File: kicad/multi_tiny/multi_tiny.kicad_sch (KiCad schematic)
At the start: 5 parts, among them U1 ATtiny85-20P, U2 ATtiny85-20P, U3 ATtiny85-20P, U4 CD4052B, U5 CD4052B

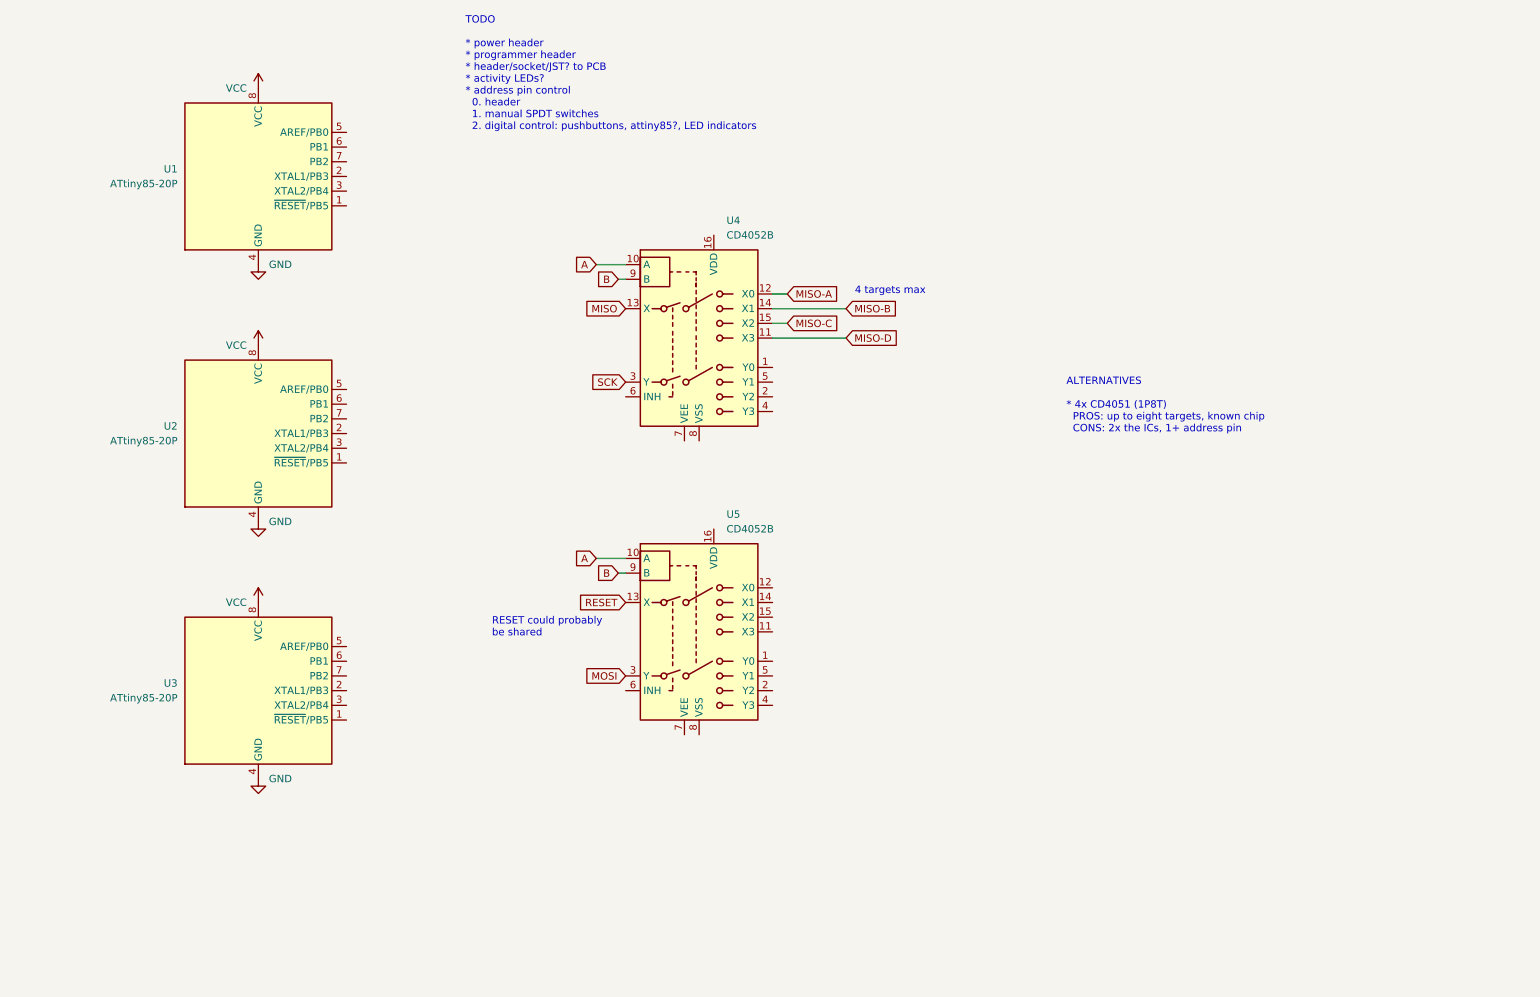
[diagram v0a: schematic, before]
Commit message: Complete MVP schematic
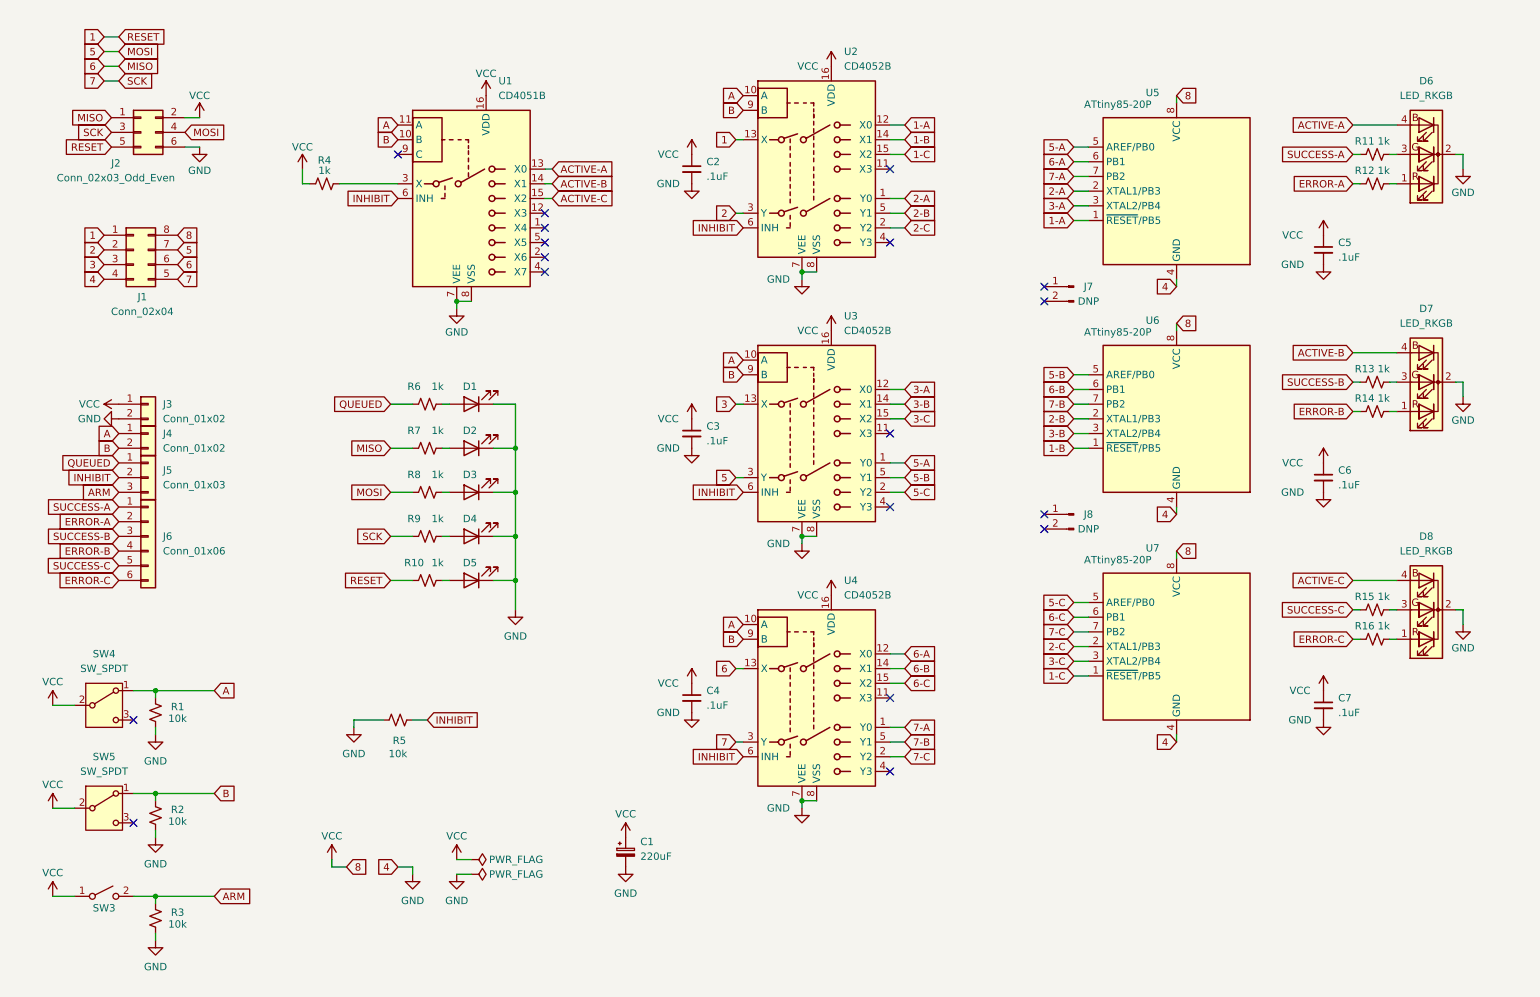
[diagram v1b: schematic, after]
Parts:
- added C1: 220uF, symbol Device:C_Polarized_Small
- added C2, C3, C4, C5, C6, C7: .1uF, symbol Device:C_Small
- added D1, D2, D3, D4, D5: LED, symbol Device:LED
- added D6, D7, D8: LED_RKGB, symbol Device:LED_RKGB
- added J1: Conn_02x04, symbol Connector_Generic:Conn_02x04_Counter_Clockwise
- added J2: Conn_02x03_Odd_Even, symbol Connector_Generic:Conn_02x03_Odd_Even
- added J3, J4: Conn_01x02, symbol Connector_Generic:Conn_01x02
- added J5: Conn_01x03, symbol Connector_Generic:Conn_01x03
- added J6: Conn_01x06, symbol Connector_Generic:Conn_01x06
- added J7, J8: DNP, symbol Connector:Conn_01x02_Pin
- added R1, R2, R3, R5: 10k, symbol Device:R_Small_US
- added R10, R11, R12, R13, R14, R15, R16, R4, R6, R7, R8, R9: 1k, symbol Device:R_Small_US
- added SW3: SW_SPST, symbol Switch:SW_SPST
- added SW4, SW5: SW_SPDT, symbol Switch:SW_SPDT
- added U1: CD4051B, symbol Analog_Switch:CD4051B
- added U4: CD4052B, symbol Analog_Switch:CD4052B
- renumbered U4 to U2, U5 to U3, U1 to U5, U2 to U6, U3 to U7
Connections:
- net MISO-A is gone; now on net 1-A: U2.12 (X0)
- net MISO-B is gone; now on net 1-B: U2.14 (X1)
- net MISO-C is gone; now on net 1-C: U2.15 (X2)
- net A: now also J4.1 (Pin_1), R1.2, SW4.1 (A), U1.11 (A), U4.10 (A)
- net B: now also J4.2 (Pin_2), R2.2, SW5.1 (A), U1.10 (B), U4.9 (B)
- net GND: now also U2.7 (VEE), U2.8 (VSS), U3.7 (VEE), U3.8 (VSS), C1.2, C2.2, C3.2, C4.2, C5.2, C6.2, C7.2, D1.1 (K), D2.1 (K), D3.1 (K), D4.1 (K), D5.1 (K), D6.2 (K), D7.2 (K), D8.2 (K), J1.4 (Pin_4), J2.6 (Pin_6), J3.2 (Pin_2), R1.1, R2.1, R3.1, R5.1, U1.7 (VEE), U1.8 (VSS), U4.7 (VEE), U4.8 (VSS)
- net VCC: now also U2.16 (VDD), U3.16 (VDD), C1.1, C2.1, C3.1, C4.1, C5.1, C6.1, C7.1, J1.8 (Pin_8), J2.2 (Pin_2), J3.1 (Pin_1), R4.1, SW3.1 (A), SW4.2 (B), SW5.2 (B), U1.16 (VDD), U4.16 (VDD)
- net 2-A: now reaches U2.1 (Y0)
- net 2-A: now also U5.2 (XTAL1/PB3)
- net 2-C: now reaches U2.2 (Y2)
- net 2-C: now also U7.2 (XTAL1/PB3)
- net 2-B: now reaches U2.5 (Y1)
- net 2-B: now also U6.2 (XTAL1/PB3)
- net INHIBIT: now reaches U2.6 (INH)
- net INHIBIT: now also U3.6 (INH), J5.2 (Pin_2), R5.2, U1.6 (INH), U4.6 (INH)
- net 1-C: now reaches U7.1 (~{RESET}/PB5)
- net 3-C: now reaches U7.3 (XTAL2/PB4)
- net 3-C: now also U3.15 (X2)
- net 5-C: now reaches U7.5 (AREF/PB0)
- net 5-C: now also U3.2 (Y2)
- net 6-C: now reaches U7.6 (PB1)
- net 6-C: now also U4.15 (X2)
- net 7-C: now reaches U7.7 (PB2)
- net 7-C: now also U4.2 (Y2)
- net 5-A: now reaches U3.1 (Y0)
- net 5-A: now also U5.5 (AREF/PB0)
- net 3-A: now reaches U3.12 (X0)
- net 3-A: now also U5.3 (XTAL2/PB4)
- net 3-B: now reaches U3.14 (X1)
- net 3-B: now also U6.3 (XTAL2/PB4)
- net 5-B: now reaches U3.5 (Y1)
- net 5-B: now also U6.5 (AREF/PB0)
- net 1-A: now reaches U5.1 (~{RESET}/PB5)
- net 6-A: now reaches U5.6 (PB1)
- net 6-A: now also U4.12 (X0)
- net 7-A: now reaches U5.7 (PB2)
- net 7-A: now also U4.1 (Y0)
- net 1-B: now reaches U6.1 (~{RESET}/PB5)
- net 6-B: now reaches U6.6 (PB1)
- net 6-B: now also U4.14 (X1)
- net 7-B: now reaches U6.7 (PB2)
- net 7-B: now also U4.5 (Y1)
- net MISO renamed 1
- net 1: now also J1.1 (Pin_1), J2.5 (Pin_5), R10.1
- net MISO-D: no longer names the net of U2.11 (X3)
- net MOSI renamed 5
- net 5: now also J1.7 (Pin_7), J2.4 (Pin_4), R8.1
- net RESET renamed 3
- net 3: now also J1.3 (Pin_3)
- net SCK renamed 2
- net 2: now also J1.2 (Pin_2)
- new net: D6.3 (GA), R11.2
- new net: D6.1 (RA), R12.2
- new net: D7.1 (RA), R14.2
- new net: D7.3 (GA), R13.2
- new net: D2.2 (A), R7.2
- new net: D8.1 (RA), R16.2
- new net: D8.3 (GA), R15.2
- new net: D5.2 (A), R10.2
- new net: D3.2 (A), R8.2
- new net: R4.2, U1.3 (X)
- new net: D1.2 (A), R6.2
- new net: D4.2 (A), R9.2
- new net 6: J1.6 (Pin_6), J2.1 (Pin_1), R7.1, U4.13 (X)
- new net 7: J1.5 (Pin_5), J2.3 (Pin_3), R9.1, U4.3 (Y)
- new net ACTIVE-A: D6.4 (BA), U1.13 (X0)
- new net ACTIVE-B: D7.4 (BA), U1.14 (X1)
- new net ACTIVE-C: D8.4 (BA), U1.15 (X2)
- new net ARM: J5.3 (Pin_3), R3.2, SW3.2 (B)
- new net ERROR-A: J6.2 (Pin_2), R12.1
- new net ERROR-B: J6.4 (Pin_4), R14.1
- new net ERROR-C: J6.6 (Pin_6), R16.1
- new net QUEUED: J5.1 (Pin_1), R6.1
- new net SUCCESS-A: J6.1 (Pin_1), R11.1
- new net SUCCESS-B: J6.3 (Pin_3), R13.1
- new net SUCCESS-C: J6.5 (Pin_5), R15.1
- no-connect marks 0 -> 18
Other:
- note removed: "4 targets max"
- note removed: "ALTERNATIVES * 4x CD4051 (1P8T) PROS: up to eight targets, known chip CONS: 2x the ICs, 1+ address pin"
- note removed: "RESET could probably be shared"
- note removed: "TODO * power header * programmer header * header/socket/JST? to PCB * activity LEDs? * address pin control 0. header 1. manual SPDT switches 2. digital control: pushbuttons, attiny85?, LED indicators"
- company: (none) -> tommy@oskitone.com
- title: (none) -> multi_tiny
- moved on the sheet: U2, U3, U5, U6, U7

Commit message: Swap CD4051 for another CD4052
* Simplifies BOM
* Enables arbitrary pin routing later
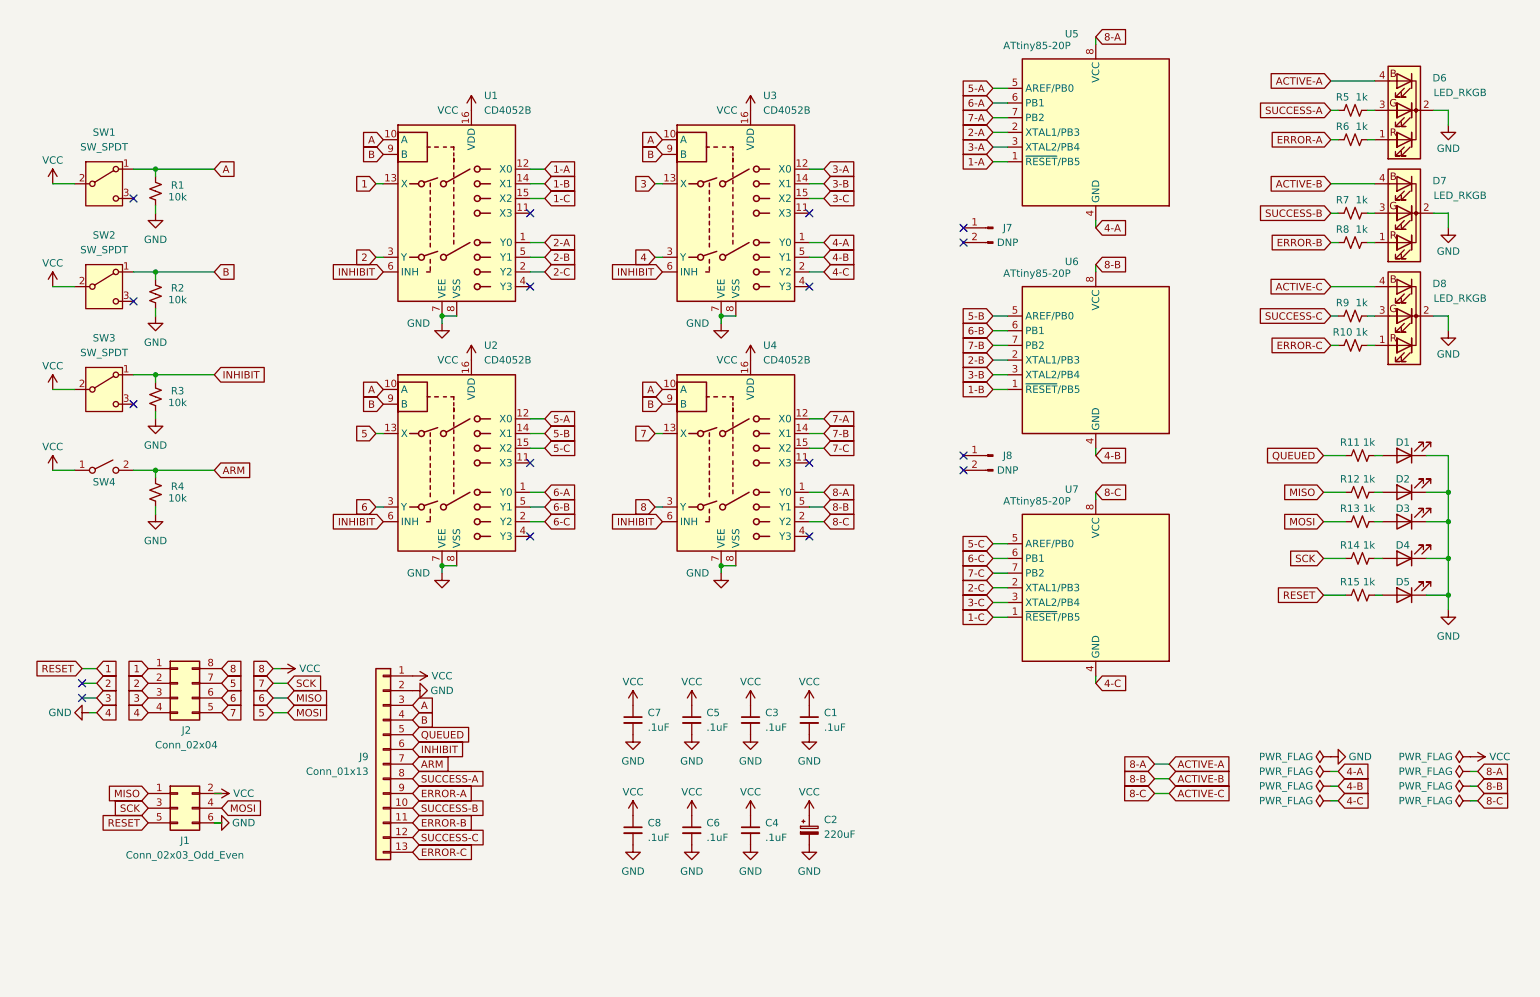
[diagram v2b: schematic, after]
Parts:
- removed C2, C3: .1uF, symbol Device:C_Small
- removed J3, J4: Conn_01x02, symbol Connector_Generic:Conn_01x02
- removed J5: Conn_01x03, symbol Connector_Generic:Conn_01x03
- removed J6: Conn_01x06, symbol Connector_Generic:Conn_01x06
- removed R10, R4, R6, R7, R8, R9: 1k, symbol Device:R_Small_US
- removed R5: 10k, symbol Device:R_Small_US
- removed U1: CD4051B, symbol Analog_Switch:CD4051B
- added C1, C5, C8: .1uF, symbol Device:C_Small
- added J9: Conn_01x13, symbol Connector_Generic:Conn_01x13
- added R11, R12, R13, R14, R15: 1k, symbol Device:R_Small_US
- added R3: 10k, symbol Device:R_Small_US
- added SW3: SW_SPDT, symbol Switch:SW_SPDT
- added U4: CD4052B, symbol Analog_Switch:CD4052B
- renumbered C1 to C2, C5 to C3, J2 to J1, J1 to J2, R16 to R10, R3 to R4, R11 to R5, R12 to R6, R13 to R7, R14 to R8, R15 to R9, SW4 to SW1, SW5 to SW2, SW3 to SW4, U2 to U1, U4 to U2
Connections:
- net 1: now also R15.1
- net 5: now also U2.13 (X), R13.1; no longer U3.3 (Y)
- net 5-A: now also U2.12 (X0); no longer U3.1 (Y0)
- net 5-B: now also U2.14 (X1); no longer U3.5 (Y1)
- net 5-C: now also U2.15 (X2); no longer U3.2 (Y2)
- net 6: now also U2.3 (Y), R12.1; no longer U2.13 (X)
- net 6-A: now also U2.1 (Y0); no longer U2.12 (X0)
- net 6-B: now also U2.5 (Y1); no longer U2.14 (X1)
- net 6-C: now also U2.2 (Y2); no longer U2.15 (X2)
- net 7: now also R14.1, U4.13 (X); no longer U2.3 (Y)
- net 7-A: now also U4.12 (X0); no longer U2.1 (Y0)
- net 7-B: now also U4.14 (X1); no longer U2.5 (Y1)
- net 7-C: now also U4.15 (X2); no longer U2.2 (Y2)
- net A: now also J9.3 (Pin_3), U4.10 (A)
- net ARM: now also J9.7 (Pin_7)
- net B: now also J9.4 (Pin_4), U4.9 (B)
- net ERROR-A: now also J9.9 (Pin_9)
- net ERROR-B: now also J9.11 (Pin_11)
- net ERROR-C: now also J9.13 (Pin_13)
- net GND: now also U3.3 (Y), C1.2, C5.2, C8.2, J9.2 (Pin_2), R3.1, U4.7 (VEE), U4.8 (VSS); no longer U5.4 (GND), U6.4 (GND), U7.4 (GND)
- net INHIBIT: now also J9.6 (Pin_6), R3.2, SW3.1 (A), U4.6 (INH)
- net QUEUED: now also J9.5 (Pin_5), R11.1
- net SUCCESS-A: now also J9.8 (Pin_8)
- net SUCCESS-B: now also J9.10 (Pin_10)
- net SUCCESS-C: now also J9.12 (Pin_12)
- net VCC: now also C1.1, C5.1, C8.1, J9.1 (Pin_1), SW3.2 (B), U4.16 (VDD), U4.3 (Y); no longer U5.8 (VCC), U6.8 (VCC), U7.8 (VCC)
- net at D2.2 (A): now also R12.2
- net at D5.2 (A): now also R15.2
- net at D3.2 (A): now also R13.2
- net at D1.2 (A): now also R11.2
- net at D4.2 (A): now also R14.2
- net ACTIVE-A renamed 8-A
- net 8-A: now also U5.8 (VCC), U4.1 (Y0)
- net ACTIVE-B renamed 8-B
- net 8-B: now also U6.8 (VCC), U4.5 (Y1)
- net ACTIVE-C renamed 8-C
- net 8-C: now also U7.8 (VCC), U4.2 (Y2)
- new net 4-A: U3.1 (Y0), U5.4 (GND)
- new net 4-B: U3.5 (Y1), U6.4 (GND)
- new net 4-C: U3.2 (Y2), U7.4 (GND)
- no-connect marks 18 -> 17
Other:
- moved on the sheet: C2, C3, D1, D2, D3, D4, D5, D6, J1, J2, J7, J8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

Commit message: Swap chips for ZIF
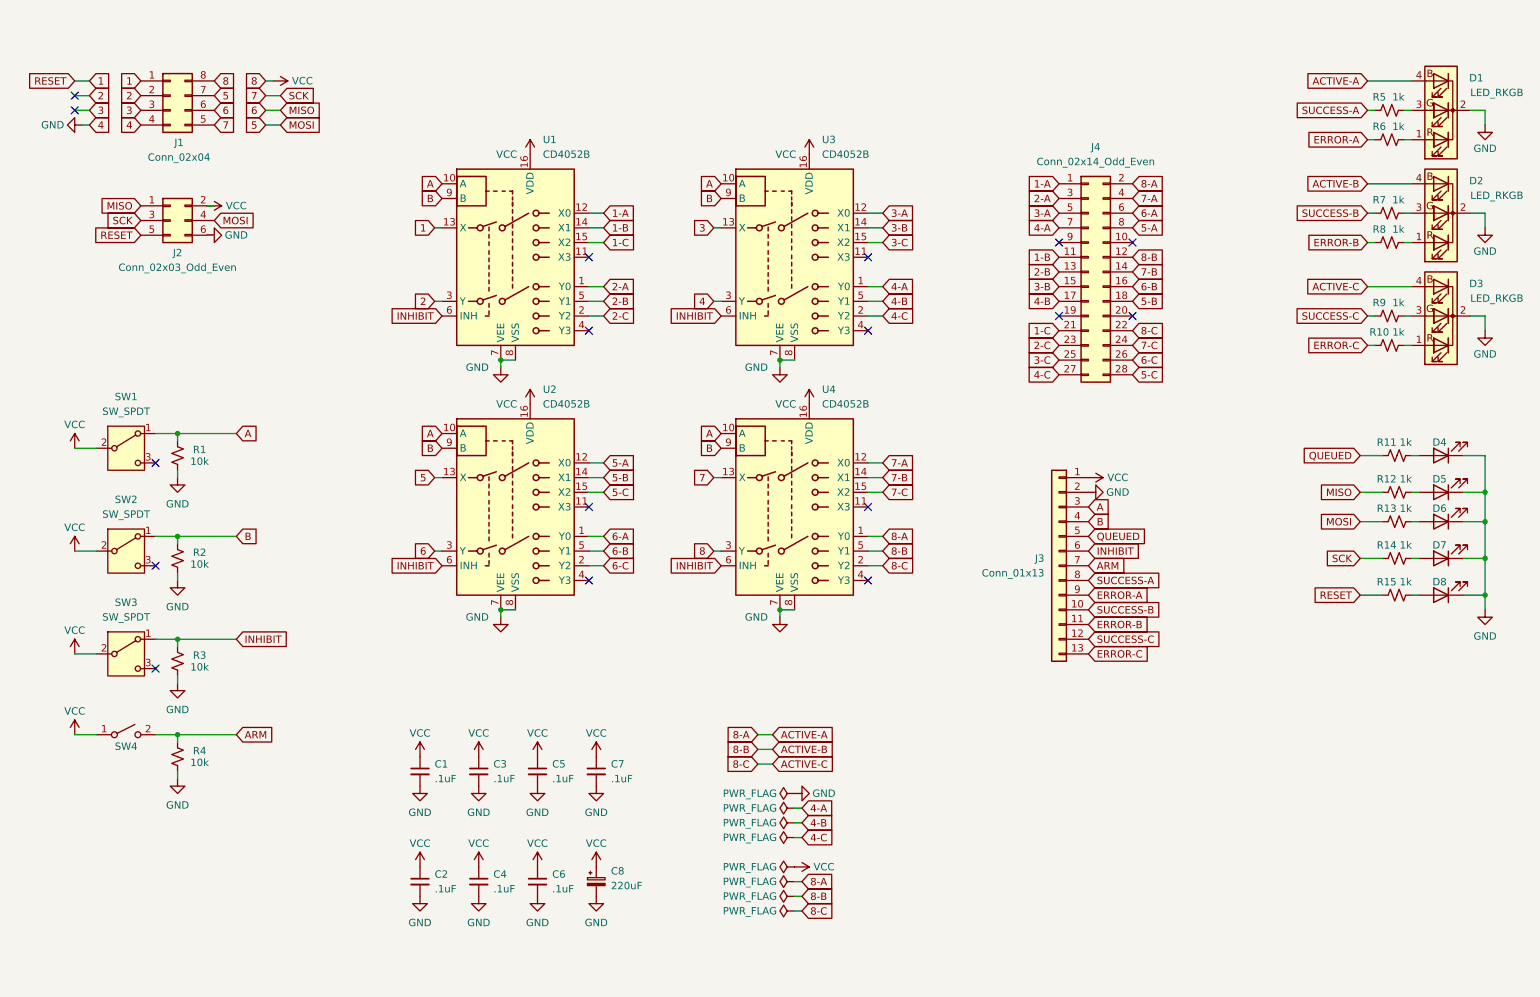
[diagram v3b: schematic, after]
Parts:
- removed J7, J8: DNP, symbol Connector:Conn_01x02_Pin
- removed U5, U6, U7: ATtiny85-20P, Package_DIP:DIP-8_W7.62mm, symbol MCU_Microchip_ATtiny:ATtiny85-20P
- added J4: Conn_02x14_Odd_Even, symbol Connector_Generic:Conn_02x14_Odd_Even
- renumbered C7 to C1, C8 to C2, C5 to C3, C6 to C4, C3 to C5, C4 to C6, C1 to C7, C2 to C8, D6 to D1, D7 to D2, D8 to D3, D1 to D4, D2 to D5, D3 to D6, D4 to D7, D5 to D8, J2 to J1, J1 to J2, J9 to J3
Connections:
- net 1-A: now also J4.1 (Pin_1)
- net 1-B: now also J4.11 (Pin_11)
- net 1-C: now also J4.21 (Pin_21)
- net 2-A: now also J4.3 (Pin_3)
- net 2-B: now also J4.13 (Pin_13)
- net 2-C: now also J4.23 (Pin_23)
- net 3-A: now also J4.5 (Pin_5)
- net 3-B: now also J4.15 (Pin_15)
- net 3-C: now also J4.25 (Pin_25)
- net 4-A: now also J4.7 (Pin_7)
- net 4-B: now also J4.17 (Pin_17)
- net 4-C: now also J4.27 (Pin_27)
- net 5-A: now also J4.8 (Pin_8)
- net 5-B: now also J4.18 (Pin_18)
- net 5-C: now also J4.28 (Pin_28)
- net 6-A: now also J4.6 (Pin_6)
- net 6-B: now also J4.16 (Pin_16)
- net 6-C: now also J4.26 (Pin_26)
- net 7-A: now also J4.4 (Pin_4)
- net 7-B: now also J4.14 (Pin_14)
- net 7-C: now also J4.24 (Pin_24)
- net 8-A: now also J4.2 (Pin_2)
- net 8-B: now also J4.12 (Pin_12)
- net 8-C: now also J4.22 (Pin_22)
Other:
- moved on the sheet: C1, C2, C3, C4, C5, C6, C7, C8, D1, D2, D3, D4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
